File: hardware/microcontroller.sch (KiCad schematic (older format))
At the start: 12 parts

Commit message: Almost finished layout
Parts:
- removed Y?: 16MHz, Crystals:Crystal_HC49-SD_SMD, symbol Crystal_Small
- added C10, C4, C6, C7, C8, C9: 100n, Capacitors_SMD:C_1210, symbol C_Small
- added C11, C3, C5: 10u, Capacitors_ThroughHole:C_Radial_D5_L11_P2, symbol CP_Small
- added D1: Status 1, Connectors_Molex:Molex_KK-6410-02_02x2.54mm_Straight, symbol Led_Small
- added D2: Status 2, Connectors_Molex:Molex_KK-6410-02_02x2.54mm_Straight, symbol Led_Small
- added R4, R5: 180R, Resistors_SMD:R_1210, symbol R
- added SW1: Reset, Buttons_Switches_SMD:SW_SPST_B3S-1000, symbol SW_PUSH_SMALL_H
- added X1: 16MHz, Crystals:crystal_FA238-TSX3225, symbol CRYSTAL_SMD
- C1, C2: renamed from C?; footprint (none) -> Capacitors_SMD:C_0603
- C12: renamed from C?; footprint (none) -> Capacitors_SMD:C_1210
- L1: renamed from L?; value Wurth 74275043 -> Wurth WE-CBF; footprint (none) -> Choke_SMD:Choke_SMD_1206_Standard
- P2: renamed from P?; value ISP -> ICSP; footprint (none) -> Pin_Headers:Pin_Header_Straight_2x03
- P4: renamed from P?; footprint (none) -> Pin_Headers:Pin_Header_Straight_2x05_Pitch1.27mm
- R1, R3, R6: renamed from R?; footprint (none) -> Resistors_SMD:R_1210
- R2: renamed from R?; value R -> 1M; footprint (none) -> Resistors_SMD:R_1210
- U1: renamed from U?; value ATMEGA32U4RC-A -> ATMEGA32U4-AU; footprint TQFP44 -> Housings_QFP:TQFP-44_10x10mm_Pitch0.8mm
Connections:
- net 3V3A: now also P2.2 (P2), P4.4 (P4), U1.24 (AVCC), U1.44 (AVCC), C10.2, C11.1, C9.2
- net 3V3D: now also U1.14 (VCC), U1.2 (UVCC), U1.34 (VCC), C5.1, C6.2, C7.2, C8.2; no longer P2.2 (P2), P4.4 (P4)
- net GND: now also U1.15 (GND), U1.23 (GND), U1.35 (GND), U1.43 (GND), U1.5 (UGND), C10.1, C11.2, C3.2, C4.2, C5.2, C6.1, C7.1, C8.1, C9.1, R4.1, R5.1, SW1.2, X1.3 (case)
- net LDR_OUT: now also U1.27 ((T0/OC4D/ADC10)PD7); no longer U1.41 ((ADC0)PF0)
- net P_OUT_1: now also U1.29 ((ADC12/OC1A/~OC4B~/PCINT12)PB5); no longer U1.26 ((T1/~OC4D~/ADC9)PD6)
- net P_OUT_2: now also U1.30 ((ADC13/OC1B/OC4B/PCINT13)PB6); no longer U1.25 ((ICP2/ADC8)PD4)
- net at C2.1, R2.2, U1.16 (XTAL2): now also X1.2
- net at C1.1, R2.1, U1.17 (XTAL1): now also X1.1
- net at R6.2: now also U1.28 ((ADC11/PCINT4)PB4); no longer U1.27 ((T0/OC4D/ADC10)PD7)
- net at U1.31 ((OC3A/~OC4A~)PC6): now also D1.2 (A)
- net at U1.32 ((ICP3/CLK0/OC4A)PC7): now also D2.2 (A)
- net at U1.42 (AREF): now also C4.1
- net at U1.6 (UCAP): now also C3.1
- net RESET renamed ~RESET
- net ~RESET: now also SW1.1
- new net: D1.1 (K), R4.2
- new net: D2.1 (K), R5.2
- no-connect marks 3 -> 15
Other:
- moved on the sheet: C1, C12, C2, R1, R2, R6

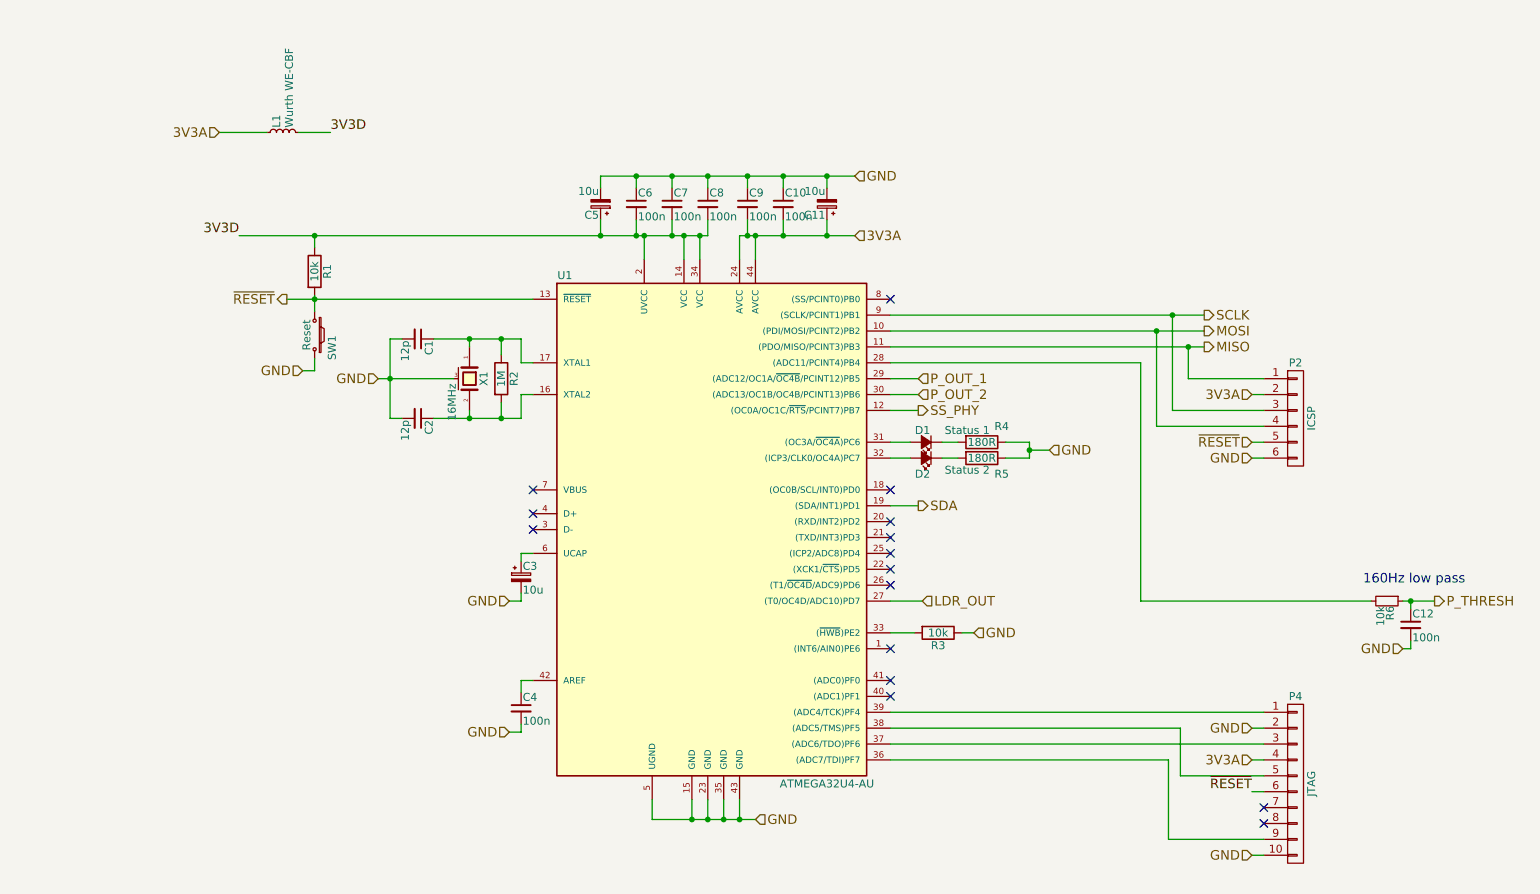
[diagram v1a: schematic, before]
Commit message: Revision of board to address issues
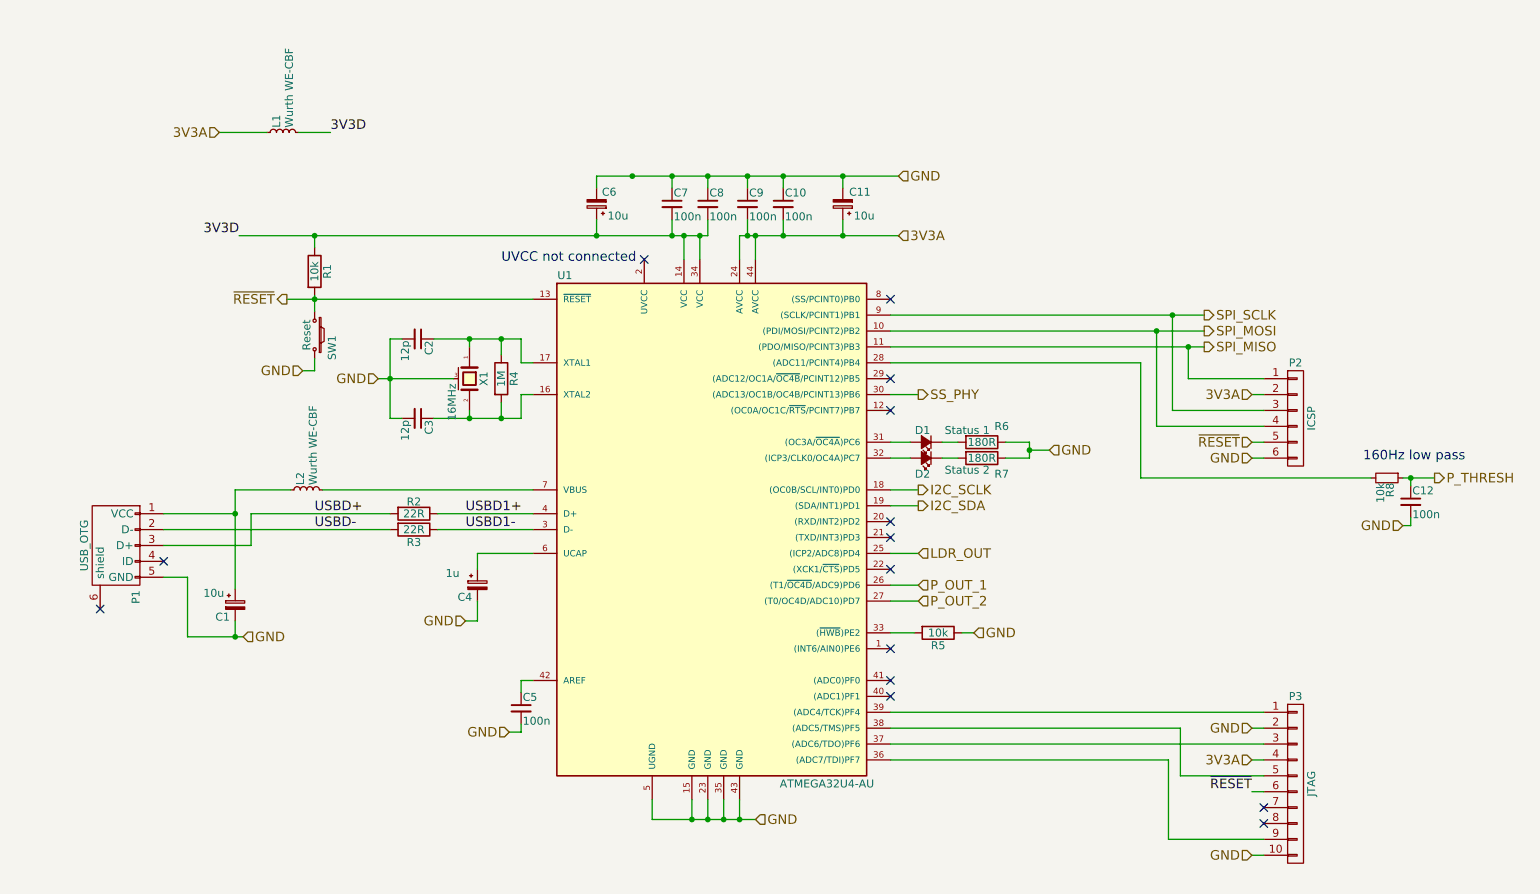
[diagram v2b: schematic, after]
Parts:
- removed C3: 10u, Capacitors_ThroughHole:C_Radial_D5_L11_P2, symbol CP_Small
- removed C6: 100n, Capacitors_SMD:C_1210, symbol C_Small
- added C1: 10u, Capacitors_ThroughHole:C_Radial_D5_L11_P2, symbol CP_Small
- added C4: 1u, Capacitors_ThroughHole:C_Radial_D5_L11_P2, symbol CP_Small
- added L2: Wurth WE-CBF, Choke_SMD:Choke_SMD_1206_Standard, symbol L_Small
- added P1: USB_OTG, Connect:USB_Micro-B_10103594-0001LF, symbol USB_OTG
- added R2, R3: 22R, Resistors_SMD:R_1206, symbol R
- C10, C12, C7, C8, C9: footprint Capacitors_SMD:C_1210 -> Capacitors_SMD:C_1206
- C5: renamed from C4; footprint Capacitors_SMD:C_1210 -> Capacitors_SMD:C_1206
- R1: footprint Resistors_SMD:R_1210 -> Resistors_SMD:R_1206
- R4: renamed from R2; footprint Resistors_SMD:R_1210 -> Resistors_SMD:R_1206
- R5: renamed from R3; footprint Resistors_SMD:R_1210 -> Resistors_SMD:R_1206
- R6: renamed from R4; footprint Resistors_SMD:R_1210 -> Resistors_SMD:R_1206
- R7: renamed from R5; footprint Resistors_SMD:R_1210 -> Resistors_SMD:R_1206
- R8: renamed from R6; footprint Resistors_SMD:R_1210 -> Resistors_SMD:R_1206
- SW1: footprint Buttons_Switches_SMD:SW_SPST_B3S-1000 -> Buttons_Switches_SMD:SW_SPST_B3SL-1002P
- renumbered C1 to C2, C2 to C3, C5 to C6, P4 to P3
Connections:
- net 3V3D: no longer U1.2 (UVCC)
- net GND: now also C1.2, C4.2, P1.5 (GND)
- net LDR_OUT: now also U1.25 ((ICP2/ADC8)PD4); no longer U1.27 ((T0/OC4D/ADC10)PD7)
- net P_OUT_1: now also U1.26 ((T1/~OC4D~/ADC9)PD6); no longer U1.29 ((ADC12/OC1A/~OC4B~/PCINT12)PB5)
- net P_OUT_2: now also U1.27 ((T0/OC4D/ADC10)PD7); no longer U1.30 ((ADC13/OC1B/OC4B/PCINT13)PB6)
- net SS_PHY: now also U1.30 ((ADC13/OC1B/OC4B/PCINT13)PB6); no longer U1.12 ((OC0A/OC1C/~RTS~/PCINT7)PB7)
- net I2C_SCLK: now reaches U1.18 ((OC0B/SCL/INT0)PD0)
- net USBD1-: now reaches U1.3 (D-)
- net USBD1-: now also R3.1
- net USBD1+: now reaches U1.4 (D+)
- net USBD1+: now also R2.1
- net at U1.6 (UCAP): now also C4.1
- net at U1.7 (VBUS): now also L2.2
- net MISO renamed SPI_MISO
- net MOSI renamed SPI_MOSI
- net SCLK renamed SPI_SCLK
- net SDA renamed I2C_SDA
- new net: C1.1, L2.1, P1.1 (VCC)
- new net USBD+: P1.3 (D+), R2.2
- new net USBD-: P1.2 (D-), R3.2
- no-connect marks 15 -> 14
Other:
- note added: "UVCC not connected"
- moved on the sheet: C11, C12, C6, R8

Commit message: Further update to change clock package and move some components around
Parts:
- SW1: footprint Buttons_Switches_SMD:SW_SPST_B3SL-1002P -> Buttons_Switches_SMD:SW_SPST_EVQP0
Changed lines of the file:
@@
 F 0 "SW1" H 3130 2635 50  0000 C CNN
 F 1 "Reset" H 3050 2475 50  0000 C CNN
-F 2 "Buttons_Switches_SMD:SW_SPST_B3SL-1002P" H 3050 2725 50  0001 C CNN
+F 2 "Buttons_Switches_SMD:SW_SPST_EVQP0" H 3050 2725 50  0001 C CNN
 F 3 "" H 3050 2725 50  0000 C CNN
 	1    3050 2525

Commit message: New revision to board
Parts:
- removed C2: 12p, Capacitors_SMD:C_0603, symbol C_Small
- removed D1: Status 1, Connectors_Molex:Molex_KK-6410-02_02x2.54mm_Straight, symbol Led_Small
- removed D2: Status 2, Connectors_Molex:Molex_KK-6410-02_02x2.54mm_Straight, symbol Led_Small
- removed L1: Wurth WE-CBF, Choke_SMD:Choke_SMD_1206_Standard, symbol L_Small
- removed R1, R5: 10k, Resistors_SMD:R_1206, symbol R
- removed R2, R3: 22R, Resistors_SMD:R_1206, symbol R
- removed R4: 1M, Resistors_SMD:R_1206, symbol R
- removed R6, R7: 180R, Resistors_SMD:R_1206, symbol R
- added C25: 12p, Capacitors_SMD:C_0603, symbol C_Small
- added L3, L4: Wurth WE-CBF, Choke_SMD:Choke_SMD_1206_Standard, symbol L_Small
- added P4: STATUS 1, Connectors_Molex:Molex_KK-6410-02_02x2.54mm_Straight, symbol CONN_01X02
- added P5: STATUS 2, Connectors_Molex:Molex_KK-6410-02_02x2.54mm_Straight, symbol CONN_01X02
- added P6: UART, Pin_Headers:Pin_Header_Straight_1x05, symbol CONN_01X05
- added R21, R25, R27, R28, R29: 10k, Resistors_SMD:R_1206, symbol R_Small
- added R22, R23: 22R, Resistors_SMD:R_1206, symbol R_Small
- added R24: 1M, Resistors_SMD:R_1206, symbol R_Small
- added R30, R31: 180R, Resistors_SMD:R_1206, symbol R_Small
- SW1: value Reset -> RESET; footprint Buttons_Switches_SMD:SW_SPST_EVQP0 -> Buttons_Switches_SMD_FSM_JSM:SW_SPST_FSM_JSM; MPN1 (none) -> 4-1437565-1; Manuf1 (none) -> TE Connectivity; SKU1 (none) -> 479-1508; Vendor1 (none) -> RS
- renumbered C1 to C24, C3 to C26, C4 to C27, C5 to C28, C6 to C29, C7 to C30, C8 to C31, C9 to C32, C10 to C33, C11 to C34, C12 to C35, P1 to P2, P2 to P3, P3 to P7, R8 to R26, U1 to U4, X1 to X2
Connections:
- net 3V3A: now also L2.1, P6.1 (P1)
- net 3V3D: now also C27.1, L2.2, U4.6 (UCAP), R21.2, R27.2, R28.2, R29.2
- net GND: now also C25.2, P6.4 (P4), R25.2, R30.1, R31.1
- net USBD+: now also R22.1
- net USBD-: now also R23.1
- net USBD1+: now also R22.2
- net USBD1-: now also R23.2
- net ~RESET: now also R21.1
- net at C26.1, U4.16 (XTAL2), X2.2: now also R24.1
- net at U4.17 (XTAL1), X2.1: now also C25.1, R24.2
- net at U4.20 ((RXD/INT2)PD2): now also P6.3 (P3)
- net at U4.21 ((TXD/INT3)PD3): now also P6.2 (P2)
- net DS18B20: now reaches U4.22 ((XCK1/~CTS~)PD5)
- net at U4.28 ((ADC11/PCINT4)PB4): no longer R26.2
- net at U4.29 ((ADC12/OC1A/~OC4B~/PCINT12)PB5): now also R26.2
- net STATUS_1: now reaches U4.31 ((OC3A/~OC4A~)PC6)
- net STATUS_1: now also P4.1 (P1)
- net STATUS_2: now reaches U4.32 ((ICP3/CLK0/OC4A)PC7)
- net STATUS_2: now also P5.1 (P1)
- net at U4.33 ((~HWB~)PE2): now also R25.1
- net ~PHY_INTERRUPT: now reaches U4.40 ((ADC1)PF1)
- net ~PHY_INTERRUPT: now also R27.1
- net ~PHY_RESET: now reaches U4.41 ((ADC0)PF0)
- net ~PHY_RESET: now also R28.1
- net at U4.7 (VBUS): now also L3.2; no longer L2.2
- net at C24.1, P2.1 (VCC): now also L3.1; no longer L2.1
- net LDR_OUT renamed LDR
- net P_OUT_1 renamed DUST_1
- net P_OUT_2 renamed DUST_2
- net P_THRESH renamed DUST_2_THRESH
- net SS_PHY renamed PHY_SS
- net PHY_SS: now also R29.1
- new net: P4.2 (P2), R30.2
- new net: P5.2 (P2), R31.2
- new net: L4.1, P6.5 (P5)
- new net 5VA: L4.2
- no-connect marks 14 -> 9
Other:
- note added: "UVCC not connected\n(see datasheet 21.3.2 fig 21-6)"
- note removed: "UVCC not connected"
- moved on the sheet: C24, C26, C27, C28, C29, C30, C31, C32, C33, C34, C35, P2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
